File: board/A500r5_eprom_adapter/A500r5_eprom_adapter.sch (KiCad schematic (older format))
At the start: 4 parts, among them U1 27C400-A500, U2 27C080-L

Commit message: Complete the schematics
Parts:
- added C1, C2: 100nF, symbol Device:C_Small
- added J1: PWR, symbol Connector:Conn_01x02_Male
- added J2: A18 Selector, symbol Connector:Conn_01x02_Male
- added J3: A19 Selector, symbol Connector:Conn_01x02_Male
- added U?: 27C080-L, symbol Memory_EPROM:27C080
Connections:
- net A0: now also U?.12 (A0)
- net A1: now also U?.11 (A1)
- net A10: now also U?.23 (A10)
- net A11: now also U?.25 (A11)
- net A12: now also U?.4 (A12)
- net A13: now also U?.28 (A13)
- net A14: now also U?.29 (A14)
- net A15: now also U?.3 (A15)
- net A16: now also U?.2 (A16)
- net A17: now also U?.30 (A17)
- net A18: now also J2.1 (Pin_1), U?.31 (A18)
- net A19: now also J3.1 (Pin_1), U?.1 (A19)
- net A2: now also U?.10 (A2)
- net A3: now also U?.9 (A3)
- net A4: now also U?.8 (A4)
- net A5: now also U?.7 (A5)
- net A6: now also U?.6 (A6)
- net A7: now also U?.5 (A7)
- net A8: now also U?.27 (A8)
- net A9: now also U?.26 (A9)
- net D0-H: now also U?.13 (D0)
- net D0-L: no longer U2.18 (D4), U2.19 (D5), U2.20 (D6), U2.21 (D7)
- net D1-H: now also U?.14 (D1)
- net D2-H: now also U?.15 (D2)
- net D3-H: now also U?.17 (D3)
- net D4-H: now also U?.18 (D4)
- net D4-L: now also U2.18 (D4)
- net D5-H: now also U?.19 (D5)
- net D5-L: now also U2.19 (D5)
- net D6-H: now also U?.20 (D6)
- net D6-L: now also U2.20 (D6)
- net D7-H: now also U?.21 (D7)
- net D7-L: now also U2.21 (D7)
- net GND: now also C1.2, C2.2, J1.2 (Pin_2), J2.2 (Pin_2), J3.2 (Pin_2), U?.16 (GND)
- net VCC: now also C1.1, C2.1, J1.1 (Pin_1), U?.32 (VCC)
- net ~CE: now also U?.22 (~CE)
- net ~OE: now also U?.24 (~OE)

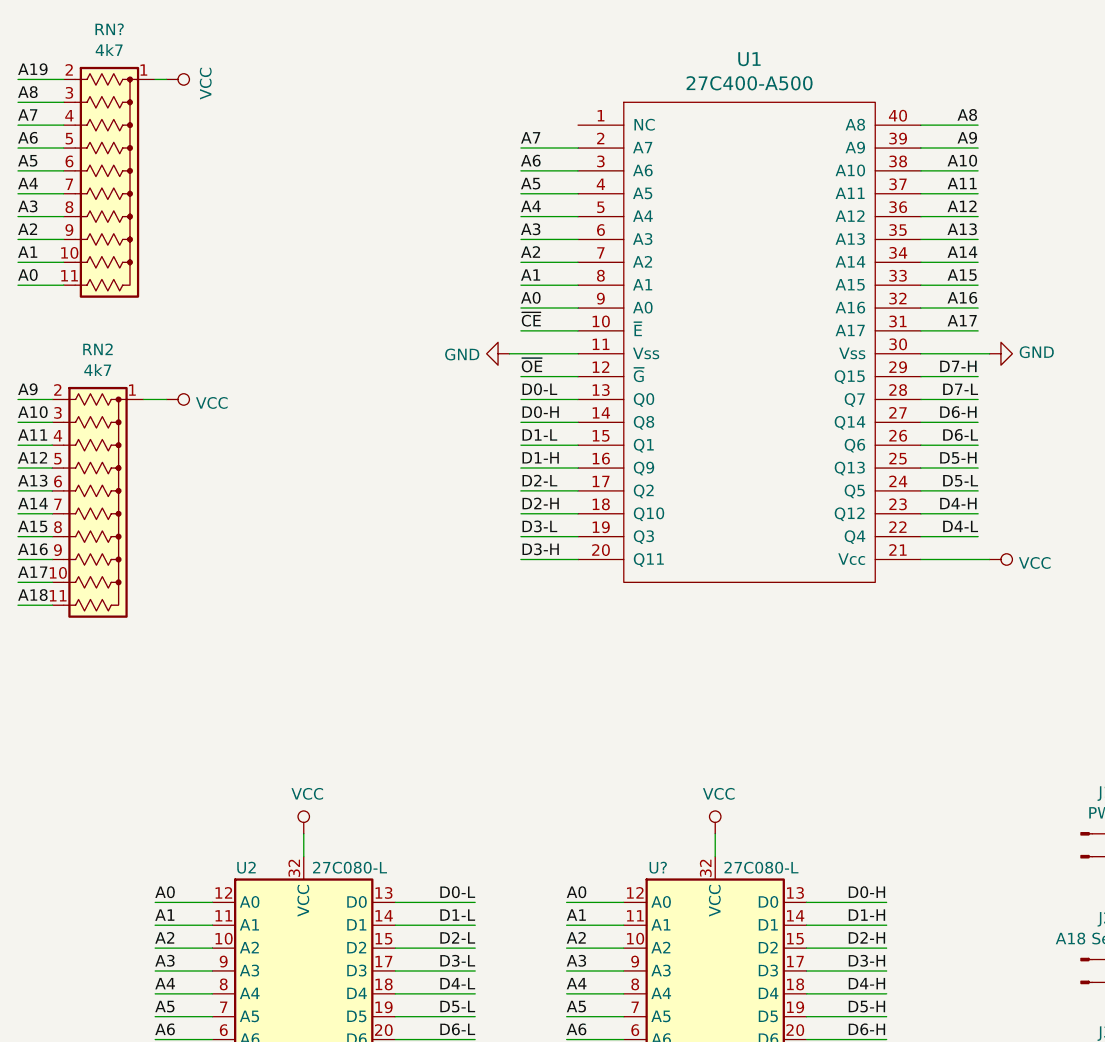
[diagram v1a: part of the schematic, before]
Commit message: Draw more of the PCB
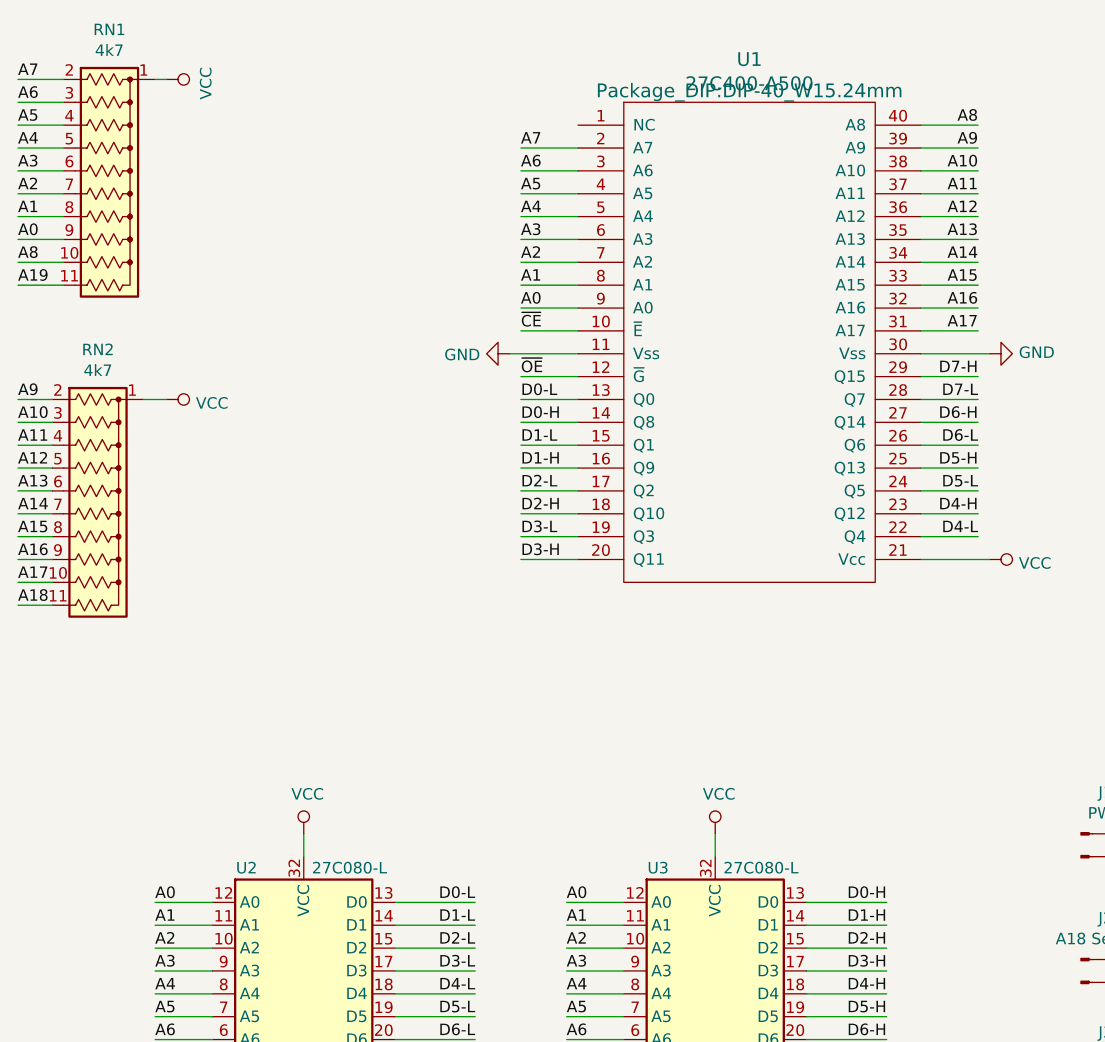
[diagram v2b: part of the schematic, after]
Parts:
- C1, C2: footprint (none) -> Capacitor_THT:C_Disc_D4.3mm_W1.9mm_P5.00mm
- J1, J2, J3: footprint (none) -> Connector_PinHeader_2.54mm:PinHeader_1x02_P2.54mm_Vertical
- U1: footprint (none) -> Package_DIP:DIP-40_W15.24mm
- U2: footprint (none) -> Package_DIP:DIP-32_W15.24mm
- U3: renamed from U?; footprint (none) -> Package_DIP:DIP-32_W15.24mm
- gave numbers to parts that had none: 1
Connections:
- net A0: now also RN1.9 (R8); no longer RN1.11 (R10)
- net A1: now also RN1.8 (R7); no longer RN1.10 (R9)
- net A19: now also RN1.11 (R10); no longer RN1.2 (R1)
- net A2: now also RN1.7 (R6); no longer RN1.9 (R8)
- net A3: now also RN1.6 (R5); no longer RN1.8 (R7)
- net A4: now also RN1.5 (R4); no longer RN1.7 (R6)
- net A5: now also RN1.4 (R3); no longer RN1.6 (R5)
- net A6: now also RN1.3 (R2); no longer RN1.5 (R4)
- net A7: now also RN1.2 (R1); no longer RN1.4 (R3)
- net A8: now also RN1.10 (R9); no longer RN1.3 (R2)
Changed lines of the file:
@@
 $EndDescr
 $Comp
-L power:VCC #PWR?
+L power:VCC #PWR0101
 U 1 1 5E28EFD0
 P 1650 1000
-F 0 "#PWR?" H 1650 850 50  0001 C CNN
+F 0 "#PWR0101" H 1650 850 50  0001 C CNN
 F 1 "VCC" H 1667 1173 50  0000 C CNN
 F 2 "" H 1650 1000 50  0001 C CNN
@@
 	1650 1000 1600 1000
 $Comp
-L power:VCC #PWR?
+L power:VCC #PWR0102
 U 1 1 5E290ED5
 P 1650 2400
-F 0 "#PWR?" H 1650 2250 50  0001 C CNN
+F 0 "#PWR0102" H 1650 2250 50  0001 C CNN
 F 1 "VCC" V 1667 2528 50  0000 L CNN
 F 2 "" H 1650 2400 50  0001 C CNN
@@
 F 0 "U1" H 4200 1187 60  0000 C CNN
 F 1 "27C400-A500" H 4200 1081 60  0000 C CNN
-F 2 "" H 4200 1050 60  0000 C CNN
+F 2 "Package_DIP:DIP-40_W15.24mm" H 4200 1050 60  0000 C CNN
 F 3 "" H 4200 1050 60  0000 C CNN
 	1    4200 1050
@@
 A0
 $Comp
-L power:GND #PWR?
+L power:GND #PWR0103
 U 1 1 5E2C8690
 P 3150 2200
-F 0 "#PWR?" H 3150 1950 50  0001 C CNN
+F 0 "#PWR0103" H 3150 1950 50  0001 C CNN
 F 1 "GND" V 3155 2072 50  0000 R CNN
 F 2 "" H 3150 2200 50  0001 C CNN
@@
 	3450 2200 3150 2200
 $Comp
-L power:GND #PWR?
+L power:GND #PWR0104
 U 1 1 5E2CB736
 P 5250 2200
-F 0 "#PWR?" H 5250 1950 50  0001 C CNN
+F 0 "#PWR0104" H 5250 1950 50  0001 C CNN
 F 1 "GND" V 5255 2072 50  0000 R CNN
 F 2 "" H 5250 2200 50  0001 C CNN
@@
 	4950 2200 5250 2200
 $Comp
-L power:VCC #PWR?
+L power:VCC #PWR0105
 U 1 1 5E2CF0CB
 P 5250 3100
-F 0 "#PWR?" H 5250 2950 50  0001 C CNN
+F 0 "#PWR0105" H 5250 2950 50  0001 C CNN
 F 1 "VCC" V 5267 3228 50  0000 L CNN
 F 2 "" H 5250 3100 50  0001 C CNN
@@
 D7-H
 $Comp
-L power:GND #PWR?
+L power:GND #PWR0106
 U 1 1 5E2F65B1
 P 2250 7100
-F 0 "#PWR?" H 2250 6850 50  0001 C CNN
+F 0 "#PWR0106" H 2250 6850 50  0001 C CNN
 F 1 "GND" H 2255 6927 50  0000 C CNN
 F 2 "" H 2250 7100 50  0001 C CNN
@@
 	2250 7000 2250 7100
 $Comp
-L power:VCC #PWR?
+L power:VCC #PWR0107
 U 1 1 5E2FBA84
 P 2250 4300
-F 0 "#PWR?" H 2250 4150 50  0001 C CNN
+F 0 "#PWR0107" H 2250 4150 50  0001 C CNN
 F 1 "VCC" H 2267 4473 50  0000 C CNN
 F 2 "" H 2250 4300 50  0001 C CNN
@@
 F 0 "U2" H 2000 6950 50  0000 C CNN
 F 1 "27C080-L" H 2450 6950 50  0000 C CNN
-F 2 "" H 2250 5700 50  0001 C CNN
+F 2 "Package_DIP:DIP-32_W15.24mm" H 2250 5700 50  0001 C CNN
 F 3 "http://ww1.microchip.com/downloads/en/devicedoc/doc0360.pdf" H 2250 5700 50  0001 C CNN
 	1    2250 5700
 	1    0    0    -1
 $EndComp
-$Comp
-L Device:R_Network10_US RN?
-U 1 1 5E3011D5
-P 1400 1500
-F 0 "RN?" V 683 1500 50  0000 C CNN
-F 1 "4k7" V 774 1500 50  0000 C CNN
-F 2 "Resistor_THT:R_Array_SIP11" V 1975 1500 50  0001 C CNN
-F 3 "http://www.vishay.com/docs/31509/csc.pdf" H 1400 1500 50  0001 C CNN
-	1    1400 1500
-	0    1    1    0
-$EndComp
+Text Label 1000 1700 0    50   ~ 0
+A0
+Text Label 1000 1600 0    50   ~ 0
+A1
+Text Label 1000 1500 0    50   ~ 0
+A2
+Text Label 1000 1400 0    50   ~ 0
+A3
+Text Label 1000 1300 0    50   ~ 0
+A4
+Text Label 1000 1200 0    50   ~ 0
+A5
+Text Label 1000 1100 0    50   ~ 0
+A6
+Text Label 1000 1000 0    50   ~ 0
+A7
+Wire Wire Line
+	1200 1700 1000 1700
+Wire Wire Line
+	1200 1600 1000 1600
+Wire Wire Line
+	1200 1500 1000 1500
+Wire Wire Line
+	1200 1400 1000 1400
+Wire Wire Line
+	1200 1300 1000 1300
+Wire Wire Line
+	1200 1200 1000 1200
+Wire Wire Line
+	1200 1100 1000 1100
+Wire Wire Line
+	1200 1000 1000 1000
+Wire Wire Line
+	1000 1900 1200 1900
 Text Label 1000 1900 0    50   ~ 0
-A0
-Text Label 1000 1800 0    50   ~ 0
-A1
-Text Label 1000 1700 0    50   ~ 0
-A2
-Text Label 1000 1600 0    50   ~ 0
-A3
-Text Label 1000 1500 0    50   ~ 0
-A4
-Text Label 1000 1400 0    50   ~ 0
-A5
-Text Label 1000 1300 0    50   ~ 0
-A6
-Text Label 1000 1200 0    50   ~ 0
-A7
-Text Label 1000 1100 0    50   ~ 0
-A8
-Wire Wire Line
-	1200 1900 1000 1900
-Wire Wire Line
-	1200 1800 1000 1800
-Wire Wire Line
-	1200 1700 1000 1700
-Wire Wire Line
-	1200 1600 1000 1600
-Wire Wire Line
-	1200 1500 1000 1500
-Wire Wire Line
-	1200 1400 1000 1400
-Wire Wire Line
-	1200 1300 1000 1300
-Wire Wire Line
-	1200 1200 1000 1200
-Wire Wire Line
-	1200 1100 1000 1100
-Wire Wire Line
-	1000 1000 1200 1000
-Text Label 1000 1000 0    50   ~ 0
 A19
 Wire Wire Line
@@
 D7-L
 $Comp
-L power:GND #PWR?
+L power:GND #PWR0108
 U 1 1 5E28F9C2
 P 4050 7100
-F 0 "#PWR?" H 4050 6850 50  0001 C CNN
+F 0 "#PWR0108" H 4050 6850 50  0001 C CNN
 F 1 "GND" H 4055 6927 50  0000 C CNN
 F 2 "" H 4050 7100 50  0001 C CNN
@@
 	4050 7000 4050 7100
 $Comp
-L power:VCC #PWR?
+L power:VCC #PWR0109
 U 1 1 5E28F9CD
 P 4050 4300
-F 0 "#PWR?" H 4050 4150 50  0001 C CNN
+F 0 "#PWR0109" H 4050 4150 50  0001 C CNN
 F 1 "VCC" H 4067 4473 50  0000 C CNN
 F 2 "" H 4050 4300 50  0001 C CNN
@@
 	4050 4300 4050 4400
 $Comp
-L Memory_EPROM:27C080 U?
+L Memory_EPROM:27C080 U3
 U 1 1 5E28F9D8
 P 4050 5700
-F 0 "U?" H 3800 6950 50  0000 C CNN
+F 0 "U3" H 3800 6950 50  0000 C CNN
 F 1 "27C080-L" H 4250 6950 50  0000 C CNN
-F 2 "" H 4050 5700 50  0001 C CNN
+F 2 "Package_DIP:DIP-32_W15.24mm" H 4050 5700 50  0001 C CNN
 F 3 "http://ww1.microchip.com/downloads/en/devicedoc/doc0360.pdf" H 4050 5700 50  0001 C CNN
 	1    4050 5700
@@
 F 0 "J1" H 5758 4481 50  0000 C CNN
 F 1 "PWR" H 5758 4390 50  0000 C CNN
-F 2 "" H 5650 4300 50  0001 C CNN
+F 2 "Connector_PinHeader_2.54mm:PinHeader_1x02_P2.54mm_Vertical" H 5650 4300 50  0001 C CNN
 F 3 "~" H 5650 4300 50  0001 C CNN
 	1    5650 4300
@@
 	6000 4400 5850 4400
 $Comp
-L power:VCC #PWR?
+L power:VCC #PWR0110
 U 1 1 5E2AD6C3
 P 6000 4300
-F 0 "#PWR?" H 6000 4150 50  0001 C CNN
+F 0 "#PWR0110" H 6000 4150 50  0001 C CNN
 F 1 "VCC" V 6000 4500 50  0000 C CNN
 F 2 "" H 6000 4300 50  0001 C CNN
@@
 $EndComp
 $Comp
-L power:GND #PWR?
+L power:GND #PWR0111
 U 1 1 5E2B5B95
 P 6000 4400
-F 0 "#PWR?" H 6000 4150 50  0001 C CNN
+F 0 "#PWR0111" H 6000 4150 50  0001 C CNN
 F 1 "GND" V 6005 4272 50  0000 R CNN
 F 2 "" H 6000 4400 50  0001 C CNN
@@
 F 0 "J2" H 5758 5031 50  0000 C CNN
 F 1 "A18 Selector" H 5758 4940 50  0000 C CNN
-F 2 "" H 5650 4850 50  0001 C CNN
+F 2 "Connector_PinHeader_2.54mm:PinHeader_1x02_P2.54mm_Vertical" H 5650 4850 50  0001 C CNN
 F 3 "~" H 5650 4850 50  0001 C CNN
 	1    5650 4850
@@
 	6100 4950 5850 4950
 $Comp
-L power:GND #PWR?
+L power:GND #PWR0112
 U 1 1 5E2D665D
 P 6100 4950
-F 0 "#PWR?" H 6100 4700 50  0001 C CNN
+F 0 "#PWR0112" H 6100 4700 50  0001 C CNN
 F 1 "GND" V 6105 4822 50  0000 R CNN
 F 2 "" H 6100 4950 50  0001 C CNN
@@
 F 0 "J3" H 5758 5531 50  0000 C CNN
 F 1 "A19 Selector" H 5758 5440 50  0000 C CNN
-F 2 "" H 5650 5350 50  0001 C CNN
+F 2 "Connector_PinHeader_2.54mm:PinHeader_1x02_P2.54mm_Vertical" H 5650 5350 50  0001 C CNN
 F 3 "~" H 5650 5350 50  0001 C CNN
 	1    5650 5350
@@
 	6100 5450 5850 5450
 $Comp
-L power:GND #PWR?
+L power:GND #PWR0113
 U 1 1 5E2D6DA2
 P 6100 5450
-F 0 "#PWR?" H 6100 5200 50  0001 C CNN
+F 0 "#PWR0113" H 6100 5200 50  0001 C CNN
 F 1 "GND" V 6105 5322 50  0000 R CNN
 F 2 "" H 6100 5450 50  0001 C CNN
@@
 F 0 "C1" H 7492 4946 50  0000 L CNN
 F 1 "100nF" H 7492 4855 50  0000 L CNN
-F 2 "" H 7400 4900 50  0001 C CNN
+F 2 "Capacitor_THT:C_Disc_D4.3mm_W1.9mm_P5.00mm" H 7400 4900 50  0001 C CNN
 F 3 "~" H 7400 4900 50  0001 C CNN
 	1    7400 4900
@@
 F 0 "C2" H 7942 4946 50  0000 L CNN
 F 1 "100nF" H 7942 4855 50  0000 L CNN
-F 2 "" H 7850 4900 50  0001 C CNN
+F 2 "Capacitor_THT:C_Disc_D4.3mm_W1.9mm_P5.00mm" H 7850 4900 50  0001 C CNN
 F 3 "~" H 7850 4900 50  0001 C CNN
 	1    7850 4900
@@
 $EndComp
 $Comp
-L power:GND #PWR?
+L power:GND #PWR0114
 U 1 1 5E2E1F49
 P 8250 5050
-F 0 "#PWR?" H 8250 4800 50  0001 C CNN
+F 0 "#PWR0114" H 8250 4800 50  0001 C CNN
 F 1 "GND" H 8300 4900 50  0000 R CNN
 F 2 "" H 8250 5050 50  0001 C CNN
@@
 $EndComp
 $Comp
-L power:VCC #PWR?
+L power:VCC #PWR0115
 U 1 1 5E2EAF33
 P 8250 4750
-F 0 "#PWR?" H 8250 4600 50  0001 C CNN
+F 0 "#PWR0115" H 8250 4600 50  0001 C CNN
 F 1 "VCC" H 8267 4923 50  0000 C CNN
 F 2 "" H 8250 4750 50  0001 C CNN
@@
 	7850 4800 7400 4800
 Connection ~ 7850 4800
+$Comp
+L Device:R_Network10_US RN1
+U 1 1 5E3011D5
+P 1400 1500
+F 0 "RN1" V 683 1500 50  0000 C CNN
+F 1 "4k7" V 774 1500 50  0000 C CNN
+F 2 "Resistor_THT:R_Array_SIP11" V 1975 1500 50  0001 C CNN
+F 3 "http://www.vishay.com/docs/31509/csc.pdf" H 1400 1500 50  0001 C CNN
+	1    1400 1500
+	0    1    1    0
+$EndComp
+Wire Wire Line
+	1200 1800 1000 1800
+Text Label 1000 1800 0    50   ~ 0
+A8
 $EndSCHEMATC

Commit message: add rev 1 for DIP adapter
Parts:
- removed J1: PWR, Connector_PinHeader_2.54mm:PinHeader_1x02_P2.54mm_Vertical, symbol Connector:Conn_01x02_Male
- added R1, R2: 4k7, Resistor_THT:R_Axial_DIN0204_L3.6mm_D1.6mm_P7.62mm_Horizontal, symbol Device:R_Small
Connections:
- net A18: now also R1.2
- net A19: now also R2.2
- net VCC: now also R1.1, R2.1
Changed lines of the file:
@@
 encoding utf-8
 Sheet 1 1
-Title ""
+Title "A500 EPROM Adapter DIP"
 Date ""
-Rev ""
+Rev "1"
 Comp ""
 Comment1 ""
@@
 D7-H
 $Comp
-L Connector:Conn_01x02_Male J1
-U 1 1 5E29DDBC
-P 5650 4300
-F 0 "J1" H 5758 4481 50  0000 C CNN
-F 1 "PWR" H 5758 4390 50  0000 C CNN
-F 2 "Connector_PinHeader_2.54mm:PinHeader_1x02_P2.54mm_Vertical" H 5650 4300 50  0001 C CNN
-F 3 "~" H 5650 4300 50  0001 C CNN
-	1    5650 4300
-	1    0    0    -1
-$EndComp
-Wire Wire Line
-	6000 4300 5850 4300
-Wire Wire Line
-	6000 4400 5850 4400
-$Comp
-L power:VCC #PWR0110
-U 1 1 5E2AD6C3
-P 6000 4300
-F 0 "#PWR0110" H 6000 4150 50  0001 C CNN
-F 1 "VCC" V 6000 4500 50  0000 C CNN
-F 2 "" H 6000 4300 50  0001 C CNN
-F 3 "" H 6000 4300 50  0001 C CNN
-	1    6000 4300
-	0    1    1    0
-$EndComp
-$Comp
-L power:GND #PWR0111
-U 1 1 5E2B5B95
-P 6000 4400
-F 0 "#PWR0111" H 6000 4150 50  0001 C CNN
-F 1 "GND" V 6005 4272 50  0000 R CNN
-F 2 "" H 6000 4400 50  0001 C CNN
-F 3 "" H 6000 4400 50  0001 C CNN
-	1    6000 4400
-	0    -1   -1   0
-$EndComp
-$Comp
 L Connector:Conn_01x02_Male J2
 U 1 1 5E2C63FF
@@
 Text Label 1000 1800 0    50   ~ 0
 A8
+$Comp
+L Device:R_Small R1
+U 1 1 5E59C5C6
+P 2150 1500
+F 0 "R1" H 2209 1546 50  0000 L CNN
+F 1 "4k7" H 2209 1455 50  0000 L CNN
+F 2 "Resistor_THT:R_Axial_DIN0204_L3.6mm_D1.6mm_P7.62mm_Horizontal" H 2150 1500 50  0001 C CNN
+F 3 "~" H 2150 1500 50  0001 C CNN
+	1    2150 1500
+	1    0    0    -1
+$EndComp
+$Comp
+L Device:R_Small R2
+U 1 1 5E59CC0A
+P 2400 1500
+F 0 "R2" H 2459 1546 50  0000 L CNN
+F 1 "4k7" H 2459 1455 50  0000 L CNN
+F 2 "Resistor_THT:R_Axial_DIN0204_L3.6mm_D1.6mm_P7.62mm_Horizontal" H 2400 1500 50  0001 C CNN
+F 3 "~" H 2400 1500 50  0001 C CNN
+	1    2400 1500
+	1    0    0    -1
+$EndComp
+Wire Wire Line
+	2150 1600 2150 1900
+Wire Wire Line
+	2400 1600 2400 1900
+Text Label 2150 1900 0    50   ~ 0
+A18
+Text Label 2400 1900 0    50   ~ 0
+A19
+Wire Wire Line
+	2150 1400 2150 1300
+Wire Wire Line
+	2150 1300 2400 1300
+Wire Wire Line
+	2400 1300 2400 1400
+$Comp
+L power:VCC #PWR?
+U 1 1 5E5B6679
+P 2400 1100
+F 0 "#PWR?" H 2400 950 50  0001 C CNN
+F 1 "VCC" H 2417 1273 50  0000 C CNN
+F 2 "" H 2400 1100 50  0001 C CNN
+F 3 "" H 2400 1100 50  0001 C CNN
+	1    2400 1100
+	1    0    0    -1
+$EndComp
+Wire Wire Line
+	2400 1100 2400 1300
+Connection ~ 2400 1300
 $EndSCHEMATC
